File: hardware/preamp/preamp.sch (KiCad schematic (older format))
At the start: 18 parts, among them J1 I/O, J4 Coil, U1 TLV170DBV

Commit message: preamp updates/minor tweaks
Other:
- moved on the sheet: J1
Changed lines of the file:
@@
 	1    0    0    -1
-$EndComp
-$Comp
-L Device:D_Schottky_ALT D1
-U 1 1 60CC8B99
-P 5350 2100
-F 0 "D1" H 5350 1883 50  0000 C CNN
-F 1 "CUS551V30,H3F" H 5350 1974 50  0000 C CNN
-F 2 "Diode_SMD:D_SOD-323" H 5350 2100 50  0001 C CNN
-F 3 "~" H 5350 2100 50  0001 C CNN
-	1    5350 2100
-	-1   0    0    1
 $EndComp
 Text GLabel 3350 4200 0    50   Input ~ 0
@@
 	1    0    0    -1
 $EndComp
-$Comp
-L power:GND #PWR0106
-U 1 1 60CDB5FB
-P 4950 2350
-F 0 "#PWR0106" H 4950 2100 50  0001 C CNN
-F 1 "GND" H 4950 2150 50  0000 C CNN
-F 2 "" H 4950 2350 50  0001 C CNN
-F 3 "" H 4950 2350 50  0001 C CNN
-	1    4950 2350
-	1    0    0    -1
-$EndComp
-Wire Wire Line
-	4950 2200 4950 2350
-$Comp
-L power:PWR_FLAG #FLG02
-U 1 1 60D52BC1
-P 5150 2350
-F 0 "#FLG02" H 5150 2425 50  0001 C CNN
-F 1 "PWR_FLAG" H 5000 2550 50  0000 C CNN
-F 2 "" H 5150 2350 50  0001 C CNN
-F 3 "~" H 5150 2350 50  0001 C CNN
-	1    5150 2350
-	-1   0    0    1
-$EndComp
-Wire Wire Line
-	5150 2350 5150 2200
-Wire Wire Line
-	5150 2200 4950 2200
-Text Notes 3800 1950 0    50   ~ 0
+Text Notes 3900 1500 0    50   ~ 0
 6, 7, 8: Main output and power\n9, 10: Mixing resistor shunt
-Text Notes 2500 1950 0    50   ~ 0
+Text Notes 2400 1500 0    50   ~ 0
 5, 4, 3: External coil\n2, 1: External coil shunt
-$Comp
-L Connector_Generic:Conn_02x05_Counter_Clockwise J1
-U 1 1 60CB8C21
-P 3550 2300
-F 0 "J1" H 3600 2717 50  0000 C CNN
-F 1 "I/O" H 3600 2626 50  0000 C CNN
-F 2 "cycfi_library:pin_header_2x5p_2.54mm_smd_horizontal" H 3550 2300 50  0001 C CNN
-F 3 "~" H 3550 2300 50  0001 C CNN
-	1    3550 2300
-	1    0    0    1
-$EndComp
 $Comp
 L power:GND #PWR0107
 U 1 1 60CC841D
-P 2450 2200
-F 0 "#PWR0107" H 2450 1950 50  0001 C CNN
-F 1 "GND" H 2450 2000 50  0000 C CNN
-F 2 "" H 2450 2200 50  0001 C CNN
-F 3 "" H 2450 2200 50  0001 C CNN
-	1    2450 2200
+P 2750 2150
+F 0 "#PWR0107" H 2750 1900 50  0001 C CNN
+F 1 "GND" H 2750 1950 50  0000 C CNN
+F 2 "" H 2750 2150 50  0001 C CNN
+F 3 "" H 2750 2150 50  0001 C CNN
+	1    2750 2150
 	1    0    0    -1
 $EndComp
-Text GLabel 3850 2500 2    50   Input ~ 0
+Text GLabel 3850 1700 2    50   Input ~ 0
 out
-Text GLabel 3850 2400 2    50   Input ~ 0
+Text GLabel 3850 1800 2    50   Input ~ 0
 mix
-Text GLabel 3850 2300 2    50   Input ~ 0
+Text GLabel 3850 1900 2    50   Input ~ 0
 mix
 Text GLabel 3350 2100 0    50   Input ~ 0
 ext_coil+
-Text GLabel 3350 2300 0    50   Input ~ 0
+Text GLabel 3350 1900 0    50   Input ~ 0
 ext_coil-
-Text GLabel 3350 2400 0    50   Input ~ 0
+Text GLabel 3350 1800 0    50   Input ~ 0
 ext_coil-
-Text GLabel 3350 2500 0    50   Input ~ 0
+Text GLabel 3350 1700 0    50   Input ~ 0
 ext_coil+
 $Comp
@@
 Wire Wire Line
 	5200 2100 3850 2100
-Wire Wire Line
-	3850 2200 4950 2200
-Connection ~ 4950 2200
-Wire Wire Line
-	3350 2200 2450 2200
 Text Label 3900 2100 0    50   ~ 0
 VCC
@@
 Wire Wire Line
 	8750 4550 8950 4550
+$Comp
+L Connector_Generic:Conn_02x05_Counter_Clockwise J1
+U 1 1 60CB8C21
+P 3550 1900
+F 0 "J1" H 3600 2317 50  0000 C CNN
+F 1 "I/O" H 3600 2226 50  0000 C CNN
+F 2 "cycfi_library:pin_header_2x5p_2.54mm_smd_horizontal" H 3550 1900 50  0001 C CNN
+F 3 "~" H 3550 1900 50  0001 C CNN
+	1    3550 1900
+	1    0    0    -1
+$EndComp
+$Comp
+L power:PWR_FLAG #FLG02
+U 1 1 60D52BC1
+P 4450 2150
+F 0 "#FLG02" H 4450 2225 50  0001 C CNN
+F 1 "PWR_FLAG" H 4300 2350 50  0000 C CNN
+F 2 "" H 4450 2150 50  0001 C CNN
+F 3 "~" H 4450 2150 50  0001 C CNN
+	1    4450 2150
+	-1   0    0    1
+$EndComp
+$Comp
+L power:GND #PWR0106
+U 1 1 60CDB5FB
+P 4250 2150
+F 0 "#PWR0106" H 4250 1900 50  0001 C CNN
+F 1 "GND" H 4250 1950 50  0000 C CNN
+F 2 "" H 4250 2150 50  0001 C CNN
+F 3 "" H 4250 2150 50  0001 C CNN
+	1    4250 2150
+	1    0    0    -1
+$EndComp
+$Comp
+L Device:D_Schottky_ALT D1
+U 1 1 60CC8B99
+P 5350 2100
+F 0 "D1" H 5350 1883 50  0000 C CNN
+F 1 "CUS551V30,H3F" H 5350 1974 50  0000 C CNN
+F 2 "Diode_SMD:D_SOD-323" H 5350 2100 50  0001 C CNN
+F 3 "~" H 5350 2100 50  0001 C CNN
+	1    5350 2100
+	-1   0    0    1
+$EndComp
+Wire Wire Line
+	4250 2000 3850 2000
+Wire Wire Line
+	4450 2150 4450 2000
+Wire Wire Line
+	4450 2000 4250 2000
+Connection ~ 4250 2000
+Wire Wire Line
+	4250 2150 4250 2000
+Wire Wire Line
+	2750 2000 2750 2150
+Wire Wire Line
+	3350 2000 2750 2000
 $EndSCHEMATC

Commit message: Preamp updates
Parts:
- H1, H2, H3, H4: footprint cycfi_library:mounting_hole_2.1mm -> cycfi_library:mounting_hole_st1.9
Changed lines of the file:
@@
 Wire Wire Line
 	8200 3950 8500 3950
-$Comp
-L Mechanical:MountingHole H1
-U 1 1 60CC8E41
-P 8300 2100
-F 0 "H1" H 8400 2146 50  0000 L CNN
-F 1 "MountingHole" H 8400 2055 50  0000 L CNN
-F 2 "cycfi_library:mounting_hole_2.1mm" H 8300 2100 50  0001 C CNN
-F 3 "~" H 8300 2100 50  0001 C CNN
-	1    8300 2100
-	1    0    0    -1
-$EndComp
-$Comp
-L Mechanical:MountingHole H2
-U 1 1 60CC94F0
-P 8300 2300
-F 0 "H2" H 8400 2346 50  0000 L CNN
-F 1 "MountingHole" H 8400 2255 50  0000 L CNN
-F 2 "cycfi_library:mounting_hole_2.1mm" H 8300 2300 50  0001 C CNN
-F 3 "~" H 8300 2300 50  0001 C CNN
-	1    8300 2300
-	1    0    0    -1
-$EndComp
-$Comp
-L Mechanical:MountingHole H3
-U 1 1 60CCA720
-P 8300 2500
-F 0 "H3" H 8400 2546 50  0000 L CNN
-F 1 "MountingHole" H 8400 2455 50  0000 L CNN
-F 2 "cycfi_library:mounting_hole_2.1mm" H 8300 2500 50  0001 C CNN
-F 3 "~" H 8300 2500 50  0001 C CNN
-	1    8300 2500
-	1    0    0    -1
-$EndComp
-$Comp
-L Mechanical:MountingHole H4
-U 1 1 60CCABB9
-P 8300 2700
-F 0 "H4" H 8400 2746 50  0000 L CNN
-F 1 "MountingHole" H 8400 2655 50  0000 L CNN
-F 2 "cycfi_library:mounting_hole_2.1mm" H 8300 2700 50  0001 C CNN
-F 3 "~" H 8300 2700 50  0001 C CNN
-	1    8300 2700
-	1    0    0    -1
-$EndComp
 Text Notes 3900 1500 0    50   ~ 0
 6, 7, 8: Main output and power\n9, 10: Mixing resistor shunt
@@
 Wire Wire Line
 	3350 2000 2750 2000
+$Comp
+L Mechanical:MountingHole H4
+U 1 1 60CCABB9
+P 8300 2700
+F 0 "H4" H 8400 2746 50  0000 L CNN
+F 1 "MountingHole" H 8400 2655 50  0000 L CNN
+F 2 "cycfi_library:mounting_hole_st1.9" H 8300 2700 50  0001 C CNN
+F 3 "~" H 8300 2700 50  0001 C CNN
+	1    8300 2700
+	1    0    0    -1
+$EndComp
+$Comp
+L Mechanical:MountingHole H3
+U 1 1 60CCA720
+P 8300 2500
+F 0 "H3" H 8400 2546 50  0000 L CNN
+F 1 "MountingHole" H 8400 2455 50  0000 L CNN
+F 2 "cycfi_library:mounting_hole_st1.9" H 8300 2500 50  0001 C CNN
+F 3 "~" H 8300 2500 50  0001 C CNN
+	1    8300 2500
+	1    0    0    -1
+$EndComp
+$Comp
+L Mechanical:MountingHole H2
+U 1 1 60CC94F0
+P 8300 2300
+F 0 "H2" H 8400 2346 50  0000 L CNN
+F 1 "MountingHole" H 8400 2255 50  0000 L CNN
+F 2 "cycfi_library:mounting_hole_st1.9" H 8300 2300 50  0001 C CNN
+F 3 "~" H 8300 2300 50  0001 C CNN
+	1    8300 2300
+	1    0    0    -1
+$EndComp
+$Comp
+L Mechanical:MountingHole H1
+U 1 1 60CC8E41
+P 8300 2100
+F 0 "H1" H 8400 2146 50  0000 L CNN
+F 1 "MountingHole" H 8400 2055 50  0000 L CNN
+F 2 "cycfi_library:mounting_hole_st1.9" H 8300 2100 50  0001 C CNN
+F 3 "~" H 8300 2100 50  0001 C CNN
+	1    8300 2100
+	1    0    0    -1
+$EndComp
 $EndSCHEMATC

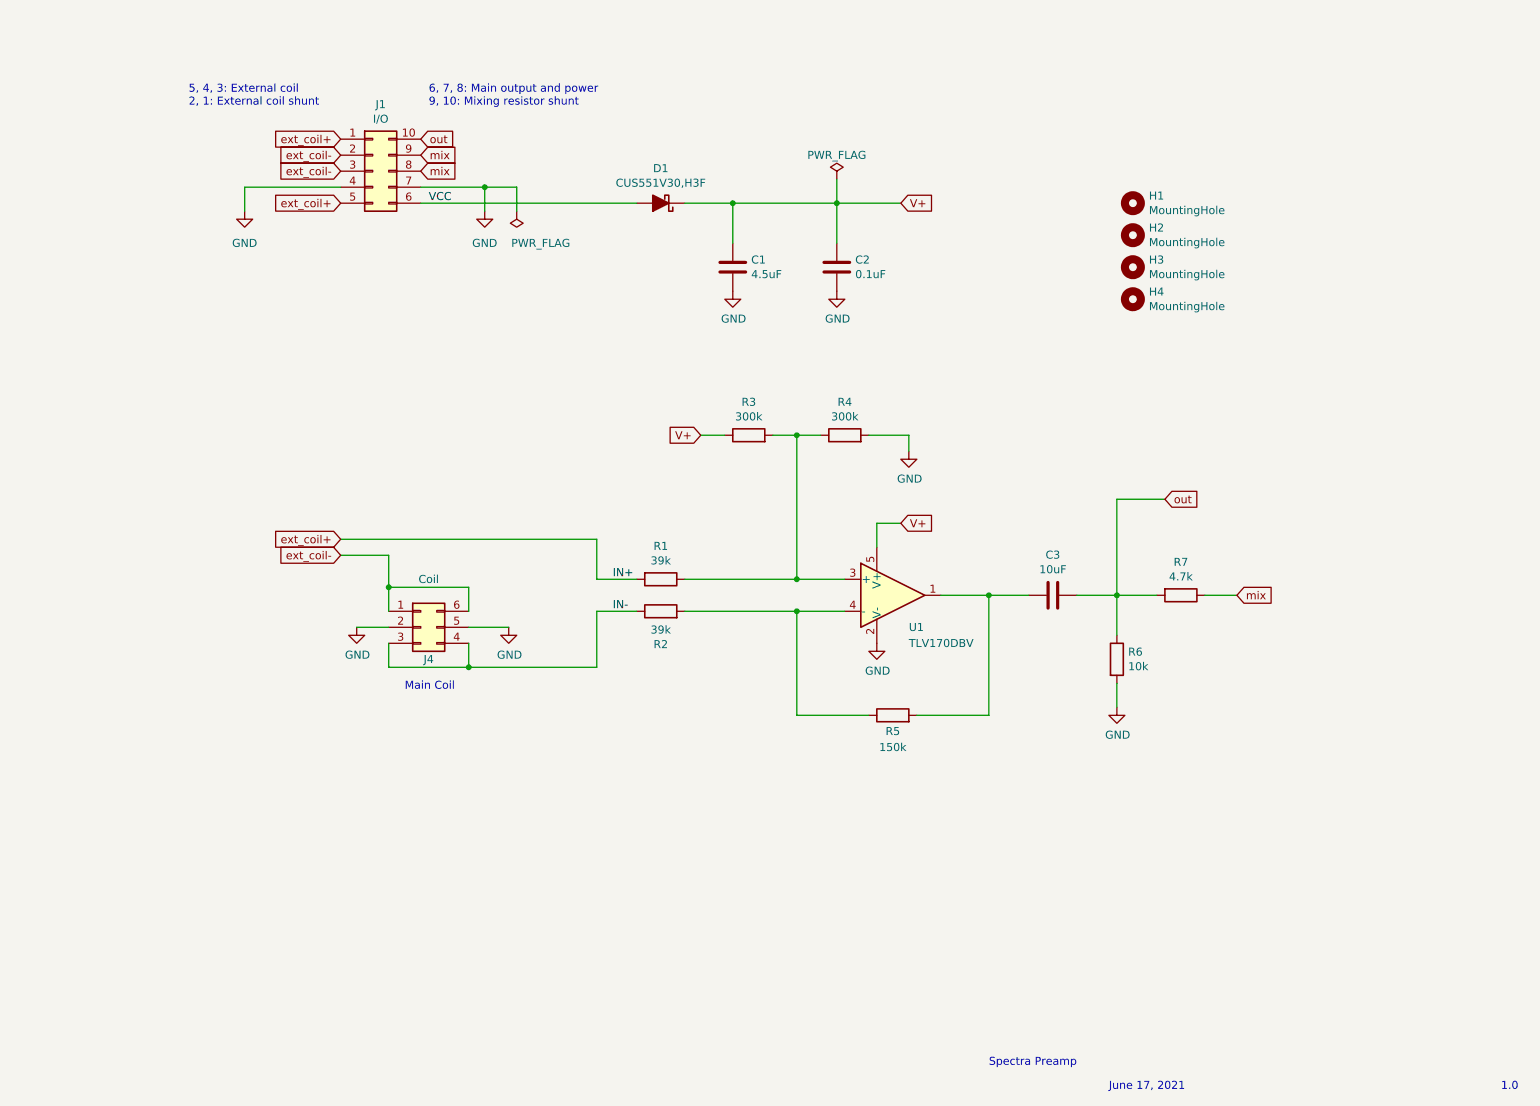
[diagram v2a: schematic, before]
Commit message: - Updated schematics (added differntial pair) - Added component reference
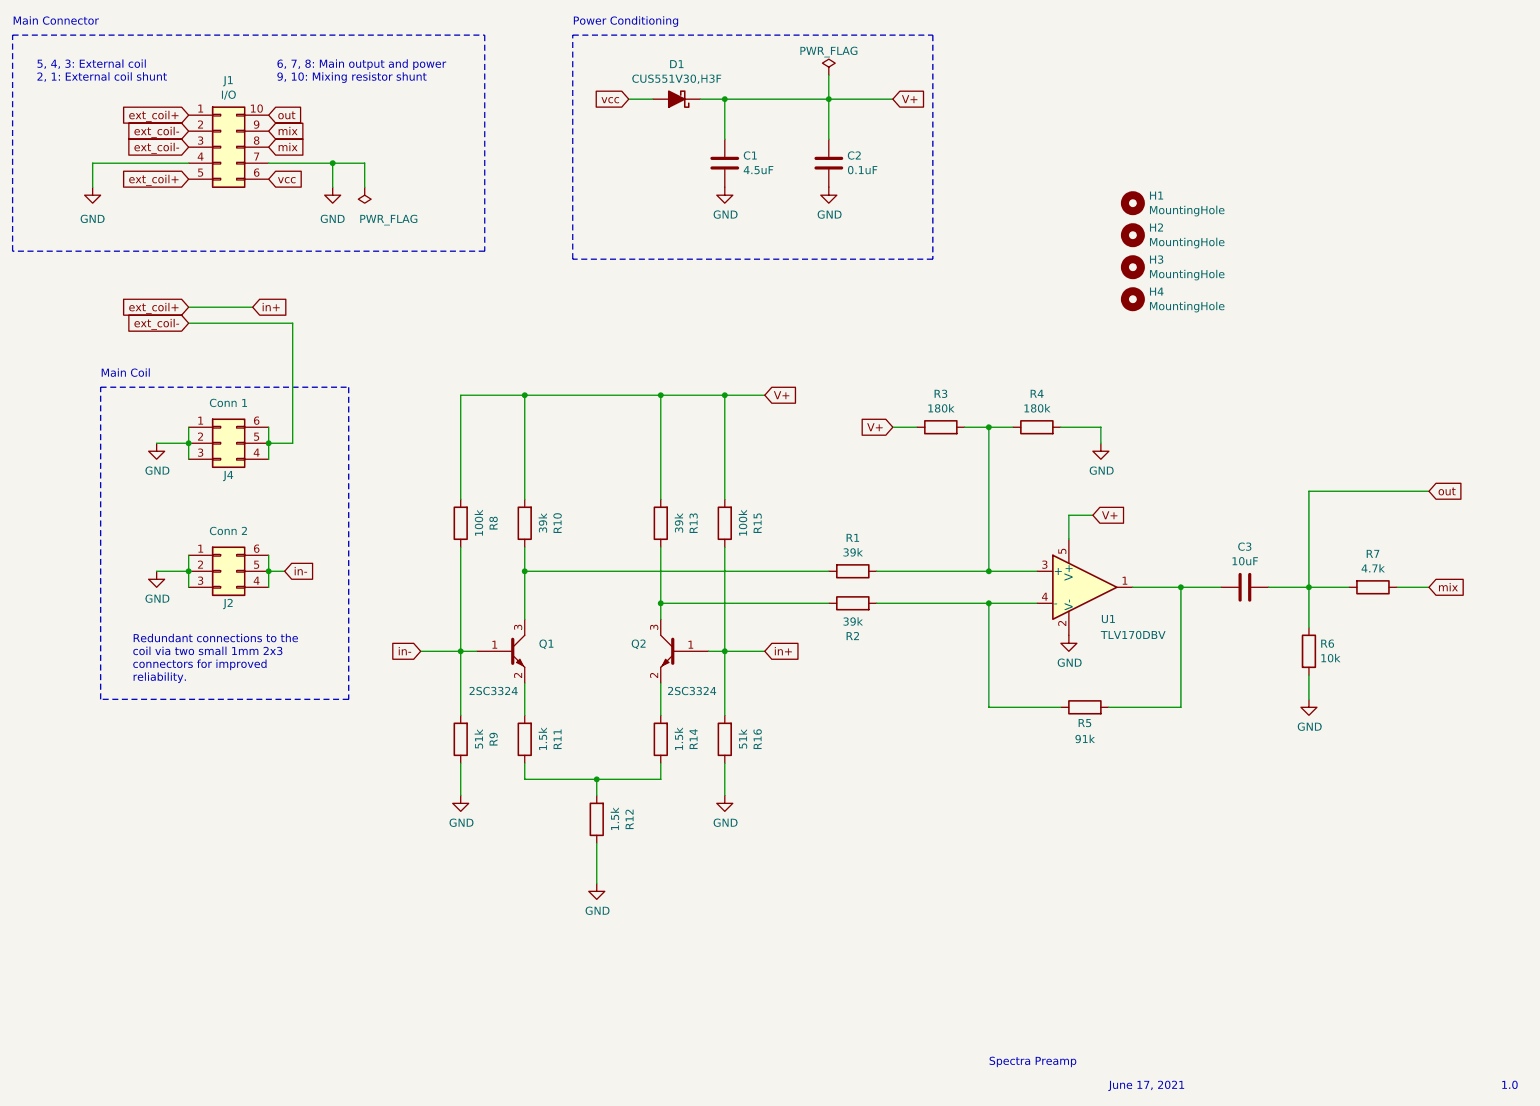
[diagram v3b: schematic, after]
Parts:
- added J2: Conn 2, cycfi_library:pin_socket_2x3p_1.00mm_smd_vertical, symbol Connector_Generic:Conn_02x03_Counter_Clockwise
- added Q1, Q2: 2SC3324, Package_TO_SOT_SMD:SOT-23, symbol cycfi_library:npn_bec
- added R10, R13: 39k, Resistor_SMD:R_0402_1005Metric, symbol Device:R
- added R11, R12, R14: 1.5k, Resistor_SMD:R_0402_1005Metric, symbol Device:R
- added R15, R8: 100k, Resistor_SMD:R_0402_1005Metric, symbol Device:R
- added R16, R9: 51k, Resistor_SMD:R_0402_1005Metric, symbol Device:R
- J4: value Coil -> Conn 1
- R3, R4: value 300k -> 180k
- R5: value 150k -> 91k
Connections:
- net GND: now also J4.1 (Pin_1), J4.3 (Pin_3), J2.1 (Pin_1), J2.2 (Pin_2), J2.3 (Pin_3), R12.1, R16.1, R9.1; no longer J4.5 (Pin_5)
- net V+: now also R10.2, R13.2, R15.2, R8.2
- net ext_coil+: now also Q2.1 (B), R15.1, R16.2; no longer R1.2
- net ext_coil-: now also J4.4 (Pin_4), J4.5 (Pin_5); no longer J4.1 (Pin_1)
- removed net IN-: J4.3 (Pin_3), J4.4 (Pin_4), R2.1
- net VCC renamed vcc
- new net: Q1.3 (C), R1.2, R10.1
- new net: Q2.3 (C), R13.1, R2.1
- new net: Q1.2 (E), R11.2
- new net: Q2.2 (E), R14.2
- new net: R11.1, R12.2, R14.1
- new net in-: J2.4 (Pin_4), J2.5 (Pin_5), J2.6 (Pin_6), Q1.1 (B), R8.1, R9.2
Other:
- note added: "Main Connector"
- note added: "Power Conditioning"
- note added: "Redundant connections to the \ncoil via two small 1mm 2x3 \nconnectors for improved \nreliability."
- moved on the sheet: C1, C2, C3, D1, J1, J4, R1, R2, R3, R4, R5, R6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
